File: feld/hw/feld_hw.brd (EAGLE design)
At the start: 30 x 30 mm, 23 parts, among them X1 PINH2X3N

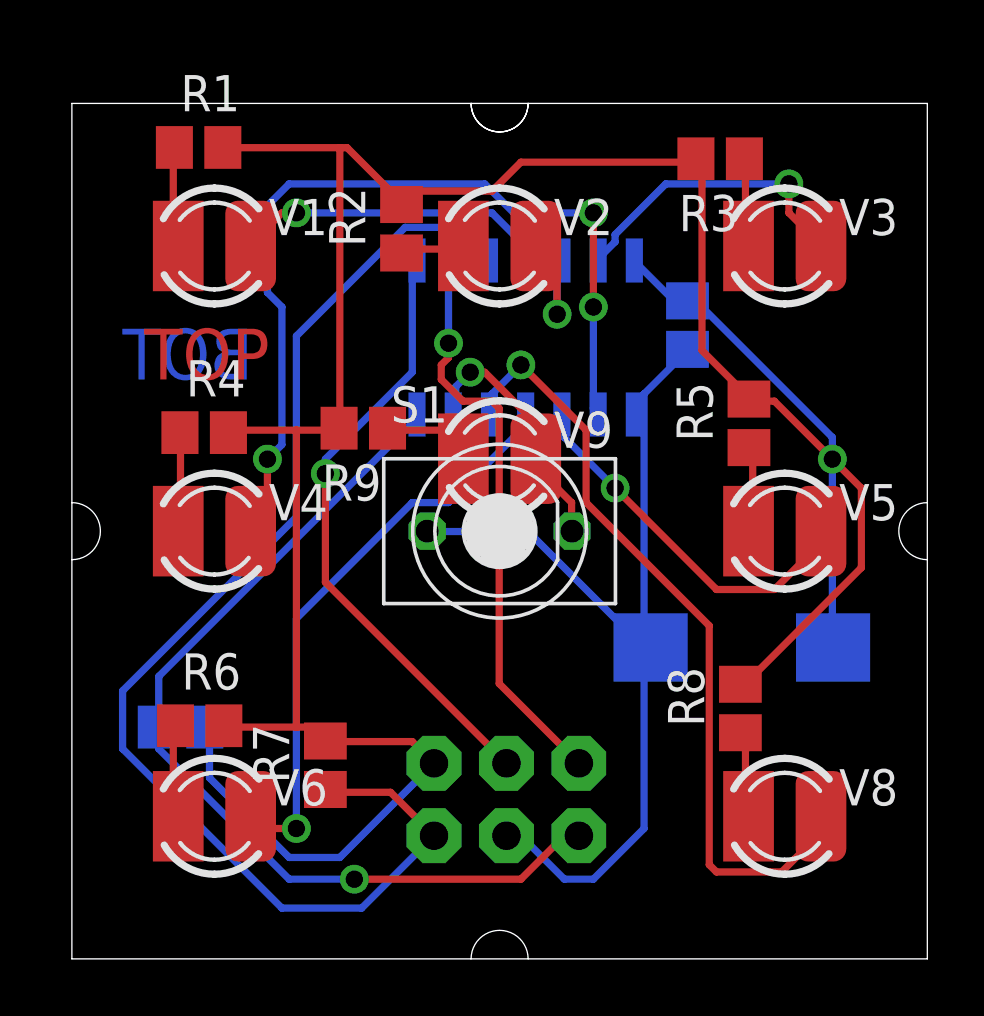
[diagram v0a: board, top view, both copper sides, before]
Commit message: 
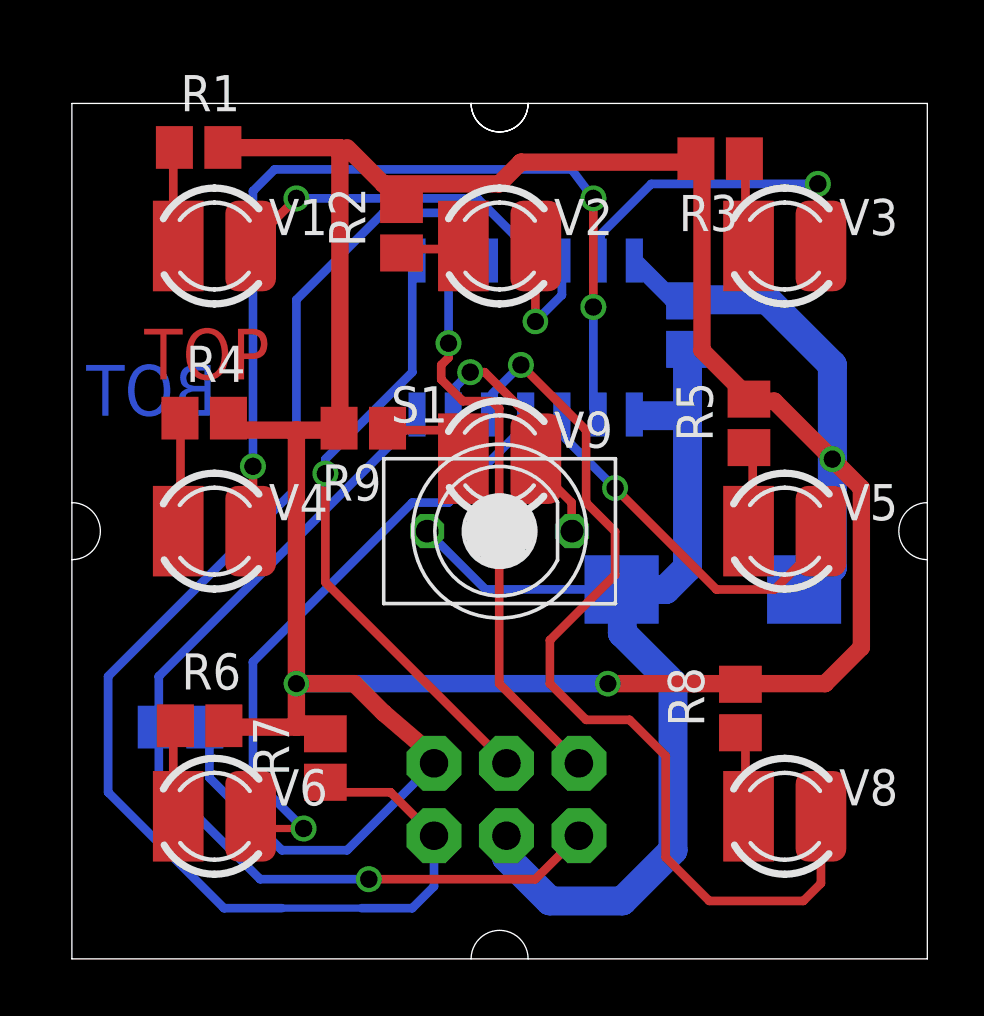
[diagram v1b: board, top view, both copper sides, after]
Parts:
- moved C2 2.27 mm to (22.5, 13.0)
- moved R4 0.51 mm to (4.64, 19.0)
- moved R7 0.25 mm to (8.89, 7.04)
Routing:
- net N$16: track 103.8 -> 124.0 mm, vias 1 -> 3
- net N$1: track 27.6 -> 33.0 mm
- net N$15: track 45.0 -> 49.0 mm
- net GND: track 34.1 -> 37.7 mm
- net N$2: track 20.5 -> 22.1 mm
- net N$6: track 4.74 -> 6.16 mm
- net N$4: track 31.4 -> 32.6 mm
- net N$5: track 10.6 -> 11.5 mm
- net N$21: track 32.9 -> 33.5 mm
- net N$11: track 3.47 -> 3.98 mm

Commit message: 
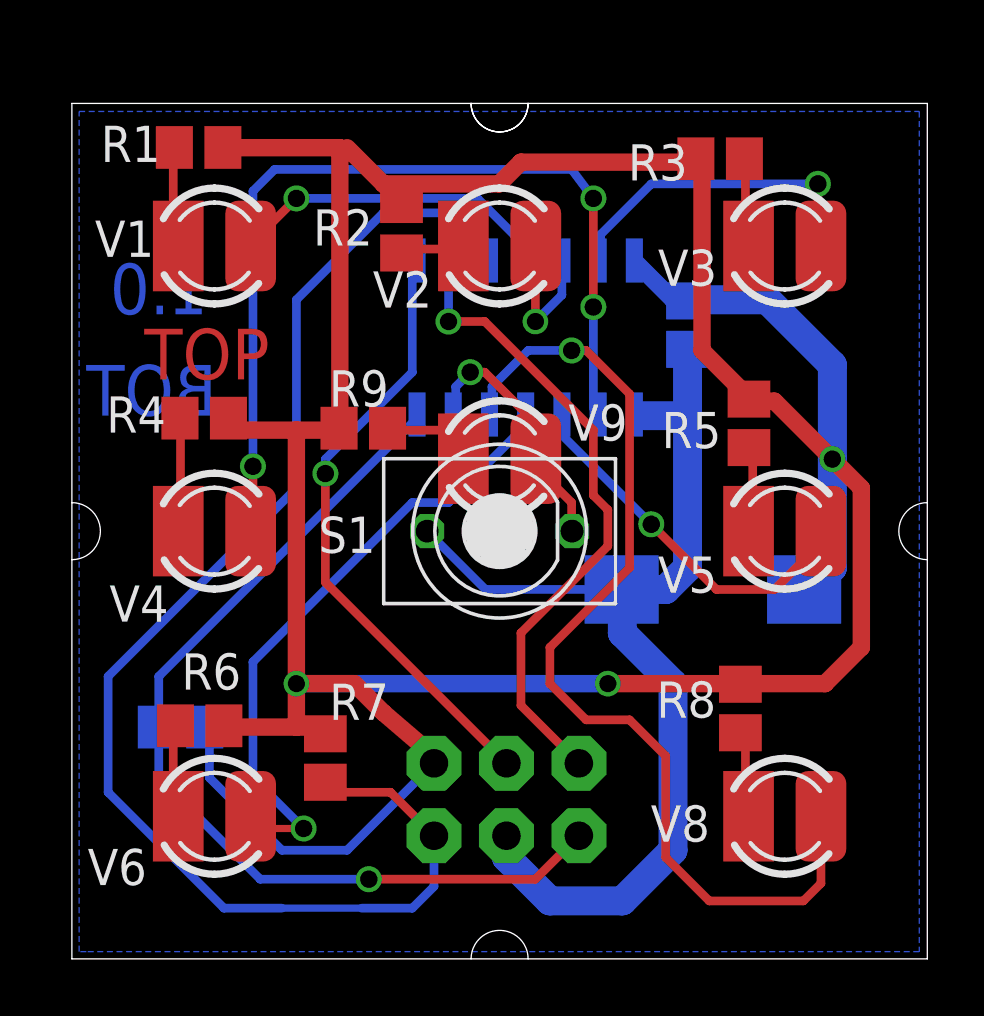
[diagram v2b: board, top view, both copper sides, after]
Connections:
- net N$15 renamed UPDI
- net N$19 renamed SCL
- net N$20 renamed SDA
- net N$21 renamed BLINK
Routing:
- net N$1: track 33.0 -> 35.6 mm
- net SCL: track 20.4 -> 22.9 mm
- added copper zone on layer 16, net GND
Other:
- board text added: "1.0"
- board text added: "BLINK"
- board text added: "GND"
- board text added: "SCL"
- board text added: "SDA"
- board text added: "UPDI"
- board text added: "VCC"

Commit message: +EDK750
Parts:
- moved C2 0.80 mm to (22.2, 12.2)
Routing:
- net GND: track 37.7 -> 39.6 mm
- net N$16: track 124.0 -> 124.8 mm
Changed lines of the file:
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@@
 <layer number="14" name="Route14" color="1" fill="6" visible="no" active="no"/>
 <layer number="15" name="Route15" color="4" fill="6" visible="no" active="no"/>
-<layer number="16" name="Bottom" color="1" fill="1" visible="no" active="yes"/>
+<layer number="16" name="Bottom" color="1" fill="1" visible="yes" active="yes"/>
 <layer number="17" name="Pads" color="2" fill="1" visible="yes" active="yes"/>
 <layer number="18" name="Vias" color="2" fill="1" visible="yes" active="yes"/>
@@
 <layer number="20" name="Dimension" color="15" fill="1" visible="yes" active="yes"/>
 <layer number="21" name="tPlace" color="7" fill="1" visible="no" active="yes"/>
-<layer number="22" name="bPlace" color="7" fill="1" visible="yes" active="yes"/>
+<layer number="22" name="bPlace" color="7" fill="1" visible="no" active="yes"/>
 <layer number="23" name="tOrigins" color="15" fill="1" visible="no" active="yes"/>
-<layer number="24" name="bOrigins" color="15" fill="1" visible="yes" active="yes"/>
+<layer number="24" name="bOrigins" color="15" fill="1" visible="no" active="yes"/>
 <layer number="25" name="tNames" color="7" fill="1" visible="no" active="yes"/>
-<layer number="26" name="bNames" color="7" fill="1" visible="yes" active="yes"/>
+<layer number="26" name="bNames" color="7" fill="1" visible="no" active="yes"/>
 <layer number="27" name="tValues" color="7" fill="1" visible="no" active="yes"/>
 <layer number="28" name="bValues" color="7" fill="1" visible="no" active="yes"/>
@@
 <layer number="49" name="Reference" color="7" fill="1" visible="yes" active="yes"/>
 <layer number="51" name="tDocu" color="7" fill="1" visible="no" active="yes"/>
-<layer number="52" name="bDocu" color="7" fill="1" visible="yes" active="yes"/>
+<layer number="52" name="bDocu" color="7" fill="1" visible="no" active="yes"/>
 <layer number="91" name="Nets" color="2" fill="1" visible="no" active="no"/>
 <layer number="92" name="Busses" color="1" fill="1" visible="no" active="no"/>
@@
 <wire x1="30" y1="16" x2="30" y2="14" width="0" layer="46" curve="180"/>
 <wire x1="14" y1="0" x2="16" y2="0" width="0" layer="46" curve="-180"/>
-<wire x1="14" y1="30" x2="16" y2="30" width="0" layer="20" curve="180"/>
+<wire x1="14" y1="30" x2="16" y2="30" width="0" layer="46" curve="180"/>
 <text x="4.826" y="22.606" size="1.778" layer="16" rot="MR0">1.0</text>
 <text x="15.494" y="8.382" size="1.016" layer="51" rot="R90">SDA</text>
@@
 <attribute name="VALUE" x="19.05" y="20.955" size="1.27" layer="28" rot="MR90"/>
 </element>
-<element name="C2" library="rclwolfi" package="CT7343" value="47µ" x="22.479" y="12.954" smashed="yes" rot="MR0">
-<attribute name="NAME" x="24.511" y="15.748" size="1.27" layer="26" rot="MR0"/>
-<attribute name="VALUE" x="25.019" y="9.144" size="1.27" layer="28" rot="MR0"/>
+<element name="C2" library="rclwolfi" package="CT7343" value="47µ" x="22.225" y="12.192" smashed="yes" rot="MR0">
+<attribute name="NAME" x="24.257" y="14.986" size="1.27" layer="26" rot="MR0"/>
+<attribute name="VALUE" x="24.765" y="8.382" size="1.27" layer="28" rot="MR0"/>
 </element>
 <element name="R10" library="rclwolfi" package="R0805" value="100k" x="3.81" y="8.128" smashed="yes" rot="MR180">
@@
 <wire x1="16.764" y1="2.032" x2="19.304" y2="2.032" width="1.016" layer="16"/>
 <wire x1="19.304" y1="2.032" x2="21.082" y2="3.81" width="1.016" layer="16"/>
-<wire x1="21.082" y1="3.81" x2="21.082" y2="9.652" width="1.016" layer="16"/>
-<wire x1="21.082" y1="9.652" x2="19.304" y2="11.43" width="1.016" layer="16"/>
-<wire x1="19.304" y1="11.43" x2="19.304" y2="12.929" width="1.016" layer="16"/>
-<wire x1="19.304" y1="12.929" x2="19.279" y2="12.954" width="1.016" layer="16"/>
-<wire x1="19.279" y1="12.954" x2="20.828" y2="12.954" width="1.016" layer="16"/>
+<wire x1="21.082" y1="3.81" x2="21.336" y2="11.938" width="1.016" layer="16"/>
+<wire x1="21.336" y1="11.938" x2="19.304" y2="12.446" width="0.3048" layer="16"/>
+<wire x1="19.304" y1="12.446" x2="19.304" y2="12.929" width="1.016" layer="16"/>
+<wire x1="19.304" y1="12.929" x2="19.025" y2="12.192" width="1.016" layer="16"/>
+<wire x1="19.025" y1="12.192" x2="20.828" y2="12.954" width="1.016" layer="16"/>
 <wire x1="20.828" y1="12.954" x2="21.59" y2="13.716" width="1.016" layer="16"/>
 <wire x1="21.59" y1="13.716" x2="21.59" y2="19.05" width="1.016" layer="16"/>
 <wire x1="21.59" y1="19.05" x2="21.59" y2="21.375" width="1.016" layer="16"/>
 <wire x1="21.55" y1="19.09" x2="21.59" y2="19.05" width="1.016" layer="16"/>
-<wire x1="19.279" y1="12.954" x2="14.506" y2="12.954" width="0.3048" layer="16"/>
+<wire x1="19.025" y1="12.192" x2="14.506" y2="12.954" width="0.3048" layer="16"/>
 <wire x1="14.506" y1="12.954" x2="12.46" y2="15" width="0.3048" layer="16"/>
 <wire x1="19.725" y1="19.09" x2="20.026" y2="19.09" width="0.3048" layer="16"/>
@@
 <wire x1="26.67" y1="17.526" x2="26.67" y2="13.716" width="1.016" layer="16"/>
 <wire x1="21.59" y1="22.86" x2="22.098" y2="22.86" width="0.254" layer="16"/>
-<wire x1="26.67" y1="13.716" x2="25.679" y2="12.954" width="1.016" layer="16"/>
+<wire x1="26.67" y1="13.716" x2="25.425" y2="12.192" width="1.016" layer="16"/>
 <wire x1="21.59" y1="22.86" x2="21.59" y2="23.075" width="0.6096" layer="16"/>
 <wire x1="24.638" y1="19.558" x2="26.67" y2="17.526" width="0.6096" layer="1"/>
